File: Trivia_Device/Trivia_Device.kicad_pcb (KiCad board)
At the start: 2 copper layers, 5 parts, among them J1 Conn_01x16, J2 Conn_01x16, J3 Conn_01x16, J4 Conn_01x16, U1 BC40C

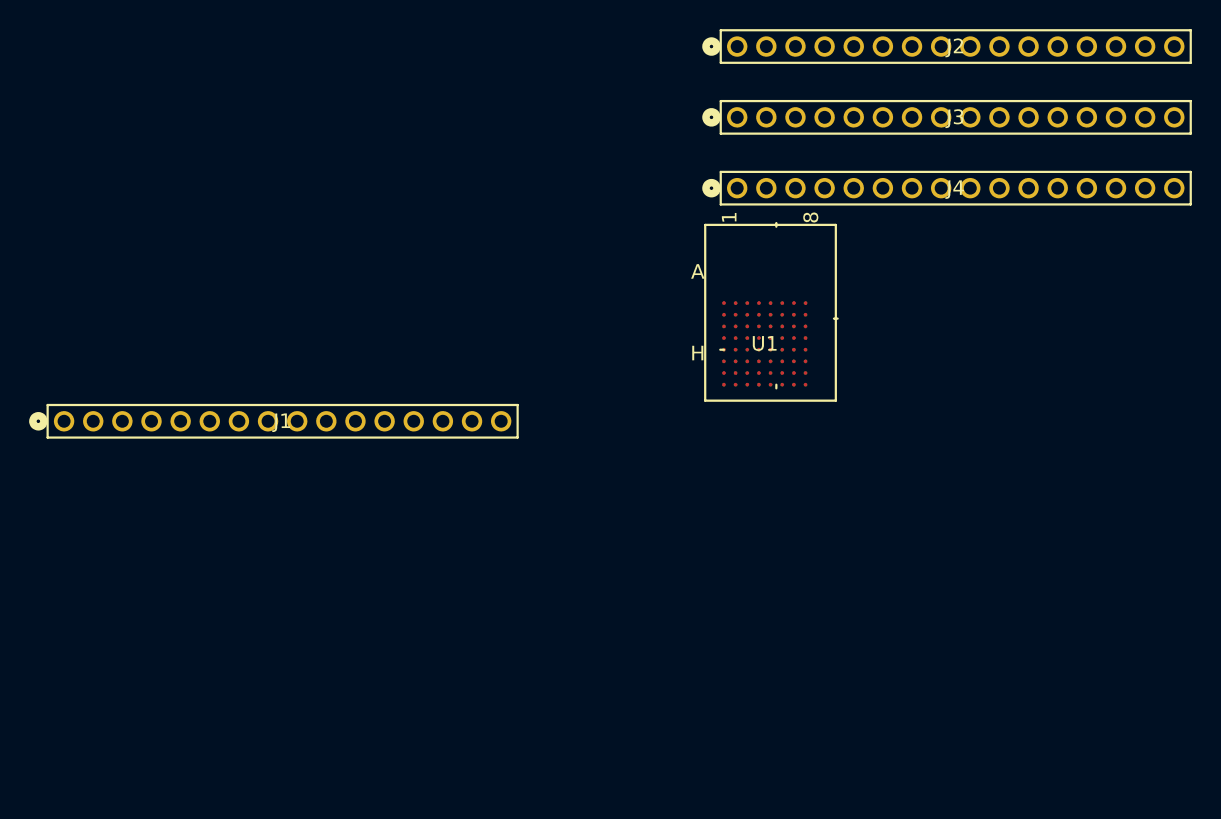
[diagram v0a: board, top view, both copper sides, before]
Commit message: working on PCB for processor board
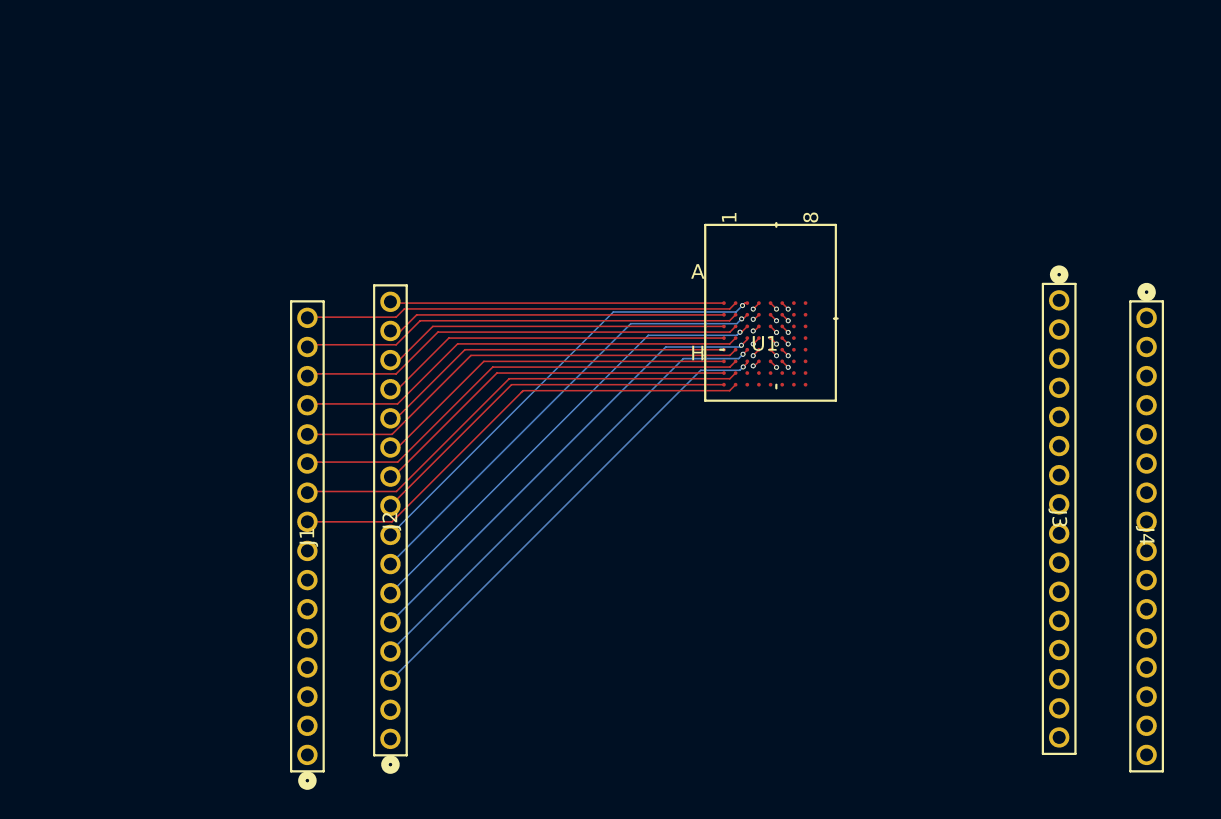
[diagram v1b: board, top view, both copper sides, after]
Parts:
- moved J2 53.1 mm to (101.8, 133.4), turned to 90 degrees
- moved J4 29.5 mm to (153.7, 104.5), turned to -90 degrees
- moved J1 28.3 mm to (96.1, 134.5), turned to 90 degrees
- moved J3 25.4 mm to (147.7, 103.3), turned to -90 degrees
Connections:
- J1 pad 1: unconnected-(J1-Pin_1-Pad1) -> D7
- J1 pad 10: unconnected-(J1-Pin_10-Pad10) -> B6
- J1 pad 11: unconnected-(J1-Pin_11-Pad11) -> B5
- J1 pad 12: unconnected-(J1-Pin_12-Pad12) -> B4
- J1 pad 13: unconnected-(J1-Pin_13-Pad13) -> B3
- J1 pad 14: unconnected-(J1-Pin_14-Pad14) -> B2
- J1 pad 15: unconnected-(J1-Pin_15-Pad15) -> B1
- J1 pad 16: unconnected-(J1-Pin_16-Pad16) -> B0
- J1 pad 2: unconnected-(J1-Pin_2-Pad2) -> D6
- J1 pad 3: unconnected-(J1-Pin_3-Pad3) -> D5
- J1 pad 4: unconnected-(J1-Pin_4-Pad4) -> D4
- J1 pad 5: unconnected-(J1-Pin_5-Pad5) -> D3
- J1 pad 6: unconnected-(J1-Pin_6-Pad6) -> D2
- J1 pad 7: unconnected-(J1-Pin_7-Pad7) -> D1
- J1 pad 8: unconnected-(J1-Pin_8-Pad8) -> D0
- J1 pad 9: unconnected-(J1-Pin_9-Pad9) -> B7
- J2 pad 1: unconnected-(J2-Pin_1-Pad1) -> C7
- J2 pad 10: unconnected-(J2-Pin_10-Pad10) -> A6
- J2 pad 11: unconnected-(J2-Pin_11-Pad11) -> A5
- J2 pad 12: unconnected-(J2-Pin_12-Pad12) -> A4
- J2 pad 13: unconnected-(J2-Pin_13-Pad13) -> A3
- J2 pad 14: unconnected-(J2-Pin_14-Pad14) -> A2
- J2 pad 15: unconnected-(J2-Pin_15-Pad15) -> A1
- J2 pad 2: unconnected-(J2-Pin_2-Pad2) -> C6
- J2 pad 3: unconnected-(J2-Pin_3-Pad3) -> C5
- J2 pad 4: unconnected-(J2-Pin_4-Pad4) -> C4
- J2 pad 5: unconnected-(J2-Pin_5-Pad5) -> C3
- J2 pad 6: unconnected-(J2-Pin_6-Pad6) -> C2
- J2 pad 7: unconnected-(J2-Pin_7-Pad7) -> C1
- J2 pad 8: A1 -> C0
- J2 pad 9: A1 -> A7
- J3 pad 1: unconnected-(J3-Pin_1-Pad1) -> H0
- J3 pad 10: unconnected-(J3-Pin_10-Pad10) -> F1
- J3 pad 11: unconnected-(J3-Pin_11-Pad11) -> F2
- J3 pad 12: unconnected-(J3-Pin_12-Pad12) -> F3
- J3 pad 13: unconnected-(J3-Pin_13-Pad13) -> F4
- J3 pad 14: unconnected-(J3-Pin_14-Pad14) -> F5
- J3 pad 15: unconnected-(J3-Pin_15-Pad15) -> F6
- J3 pad 16: unconnected-(J3-Pin_16-Pad16) -> F7
- J3 pad 2: unconnected-(J3-Pin_2-Pad2) -> H1
- J3 pad 3: unconnected-(J3-Pin_3-Pad3) -> H2
- J3 pad 4: unconnected-(J3-Pin_4-Pad4) -> H3
- J3 pad 5: unconnected-(J3-Pin_5-Pad5) -> H4
- J3 pad 6: unconnected-(J3-Pin_6-Pad6) -> H5
- J3 pad 8: unconnected-(J3-Pin_8-Pad8) -> H7
- J3 pad 9: unconnected-(J3-Pin_9-Pad9) -> F0
- J4 pad 1: unconnected-(J4-Pin_1-Pad1) -> G0
- J4 pad 10: unconnected-(J4-Pin_10-Pad10) -> E1
- J4 pad 11: unconnected-(J4-Pin_11-Pad11) -> E2
- J4 pad 12: unconnected-(J4-Pin_12-Pad12) -> E3
- J4 pad 13: unconnected-(J4-Pin_13-Pad13) -> E4
- J4 pad 14: unconnected-(J4-Pin_14-Pad14) -> E5
- J4 pad 15: unconnected-(J4-Pin_15-Pad15) -> E6
- J4 pad 16: unconnected-(J4-Pin_16-Pad16) -> E7
- J4 pad 2: unconnected-(J4-Pin_2-Pad2) -> G1
- J4 pad 3: unconnected-(J4-Pin_3-Pad3) -> G2
- J4 pad 4: unconnected-(J4-Pin_4-Pad4) -> G3
- J4 pad 5: unconnected-(J4-Pin_5-Pad5) -> G4
- J4 pad 6: unconnected-(J4-Pin_6-Pad6) -> G5
- J4 pad 8: unconnected-(J4-Pin_8-Pad8) -> G7
- J4 pad 9: unconnected-(J4-Pin_9-Pad9) -> E0
- U1 pad A2: unconnected-(U1-P020-PadA2) -> A2
- U1 pad A3: unconnected-(U1-P017/QSPI_CLK-PadA3) -> A3
- U1 pad A4: unconnected-(U1-P015/QSPI2-PadA4) -> A4
- U1 pad A5: unconnected-(U1-P013/QSPI0-PadA5) -> A5
- U1 pad A6: unconnected-(U1-P105-PadA6) -> A6
- U1 pad A7: unconnected-(U1-P106-PadA7) -> A7
- U1 pad B0: unconnected-(U1-P025/AIN4-PadB0) -> B0
- U1 pad B1: unconnected-(U1-P024-PadB1) -> B1
- U1 pad B2: unconnected-(U1-P022-PadB2) -> B2
- U1 pad B3: unconnected-(U1-P018/QSPI_CS-PadB3) -> B3
- U1 pad B4: unconnected-(U1-P014/QSPI1-PadB4) -> B4
- U1 pad B5: unconnected-(U1-P016/QSPI3-PadB5) -> B5
- U1 pad B6: unconnected-(U1-P007/AIN3-PadB6) -> B6
- U1 pad B7: unconnected-(U1-P012-PadB7) -> B7
- U1 pad C0: unconnected-(U1-P027/AIN6-PadC0) -> C0
- U1 pad C1: unconnected-(U1-P026/AIN5-PadC1) -> C1
- U1 pad C2: unconnected-(U1-P021-PadC2) -> C2
- U1 pad C3: unconnected-(U1-P019-PadC3) -> C3
- U1 pad C4: unconnected-(U1-P009-PadC4) -> C4
- U1 pad C5: unconnected-(U1-P102/I2C-PadC5) -> C5
- U1 pad C6: unconnected-(U1-P003/NFC2-PadC6) -> C6
- U1 pad C7: unconnected-(U1-P008-PadC7) -> C7
- U1 pad D0: unconnected-(U1-SWDIO-PadD0) -> D0
- U1 pad D1: unconnected-(U1-SWDCLK-PadD1) -> D1
- U1 pad D2: unconnected-(U1-/RESET-PadD2) -> D2
- U1 pad D3: unconnected-(U1-VSS-PadD3) -> D3
- U1 pad D4: unconnected-(U1-P005/AIN1-PadD4) -> D4
- U1 pad D5: unconnected-(U1-P004/AIN0-PadD5) -> D5
- U1 pad D6: unconnected-(U1-P023-PadD6) -> D6
- U1 pad D7: unconnected-(U1-P006/AIN2-PadD7) -> D7
- U1 pad E0: unconnected-(U1-GND-PadE0) -> E0
- U1 pad E1: unconnected-(U1-P029-PadE1) -> E1
- U1 pad E2: unconnected-(U1-P107-PadE2) -> E2
- U1 pad E3: unconnected-(U1-P031-PadE3) -> E3
- U1 pad E4: unconnected-(U1-P101-PadE4) -> E4
- U1 pad E5: unconnected-(U1-P100-PadE5) -> E5
- U1 pad E6: unconnected-(U1-P103/I2C-PadE6) -> E6
- U1 pad E7: unconnected-(U1-P011-PadE7) -> E7
- U1 pad F0: unconnected-(U1-GND-PadF0) -> F0
- U1 pad F1: unconnected-(U1-P028/AIN7-PadF1) -> F1
- U1 pad F2: unconnected-(U1-P108-PadF2) -> F2
- U1 pad F3: unconnected-(U1-P112-PadF3) -> F3
- U1 pad F4: unconnected-(U1-GND-PadF4) -> F4
- U1 pad F5: unconnected-(U1-VBUS-PadF5) -> F5
- U1 pad F6: unconnected-(U1-VDDH-PadF6) -> F6
- U1 pad F7: unconnected-(U1-P002/NFC1-PadF7) -> F7
- U1 pad G0: unconnected-(U1-VSS-PadG0) -> G0
- U1 pad G1: unconnected-(U1-P030-PadG1) -> G1
- U1 pad G2: unconnected-(U1-P110-PadG2) -> G2
- U1 pad G3: unconnected-(U1-P113-PadG3) -> G3
- U1 pad G4: unconnected-(U1-VDD-PadG4) -> G4
- U1 pad G5: unconnected-(U1-D--PadG5) -> G5
- U1 pad G7: unconnected-(U1-P010-PadG7) -> G7
- U1 pad H0: unconnected-(U1-GND-PadH0) -> H0
- U1 pad H1: unconnected-(U1-GND-PadH1) -> H1
- U1 pad H2: unconnected-(U1-P111-PadH2) -> H2
- U1 pad H3: unconnected-(U1-P114-PadH3) -> H3
- U1 pad H4: unconnected-(U1-P115-PadH4) -> H4
- U1 pad H5: unconnected-(U1-D+-PadH5) -> H5
- U1 pad H7: unconnected-(U1-VSS-PadH7) -> H7
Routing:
- net C5: track 0.00 -> 33.6 mm, vias 0 -> 1
- net B7: track 0.00 -> 33.3 mm
- net C4: track 0.00 -> 33.1 mm, vias 0 -> 1
- net B6: track 0.00 -> 32.9 mm
- net C3: track 0.00 -> 32.6 mm, vias 0 -> 1
- net B5: track 0.00 -> 32.3 mm
- net C2: track 0.00 -> 32.2 mm, vias 0 -> 1
- net B4: track 0.00 -> 31.8 mm
- net C1: track 0.00 -> 31.6 mm, vias 0 -> 1
- net B3: track 0.00 -> 31.3 mm
- net C0: track 0.00 -> 31.2 mm, vias 0 -> 1
- net B2: track 0.00 -> 30.8 mm
- net B1: track 0.00 -> 30.3 mm
- net B0: track 0.00 -> 29.9 mm
- net A7: track 0.00 -> 26.3 mm
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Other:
- copper layers 2 -> 4
